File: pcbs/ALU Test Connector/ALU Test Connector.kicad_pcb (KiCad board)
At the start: 2 copper layers, 137.2 x 137.2 mm, 6 parts, among them J1 Conn_02x20_Odd_Even, J2 Conn_02x20_Odd_Even, J3 Conn_01x04

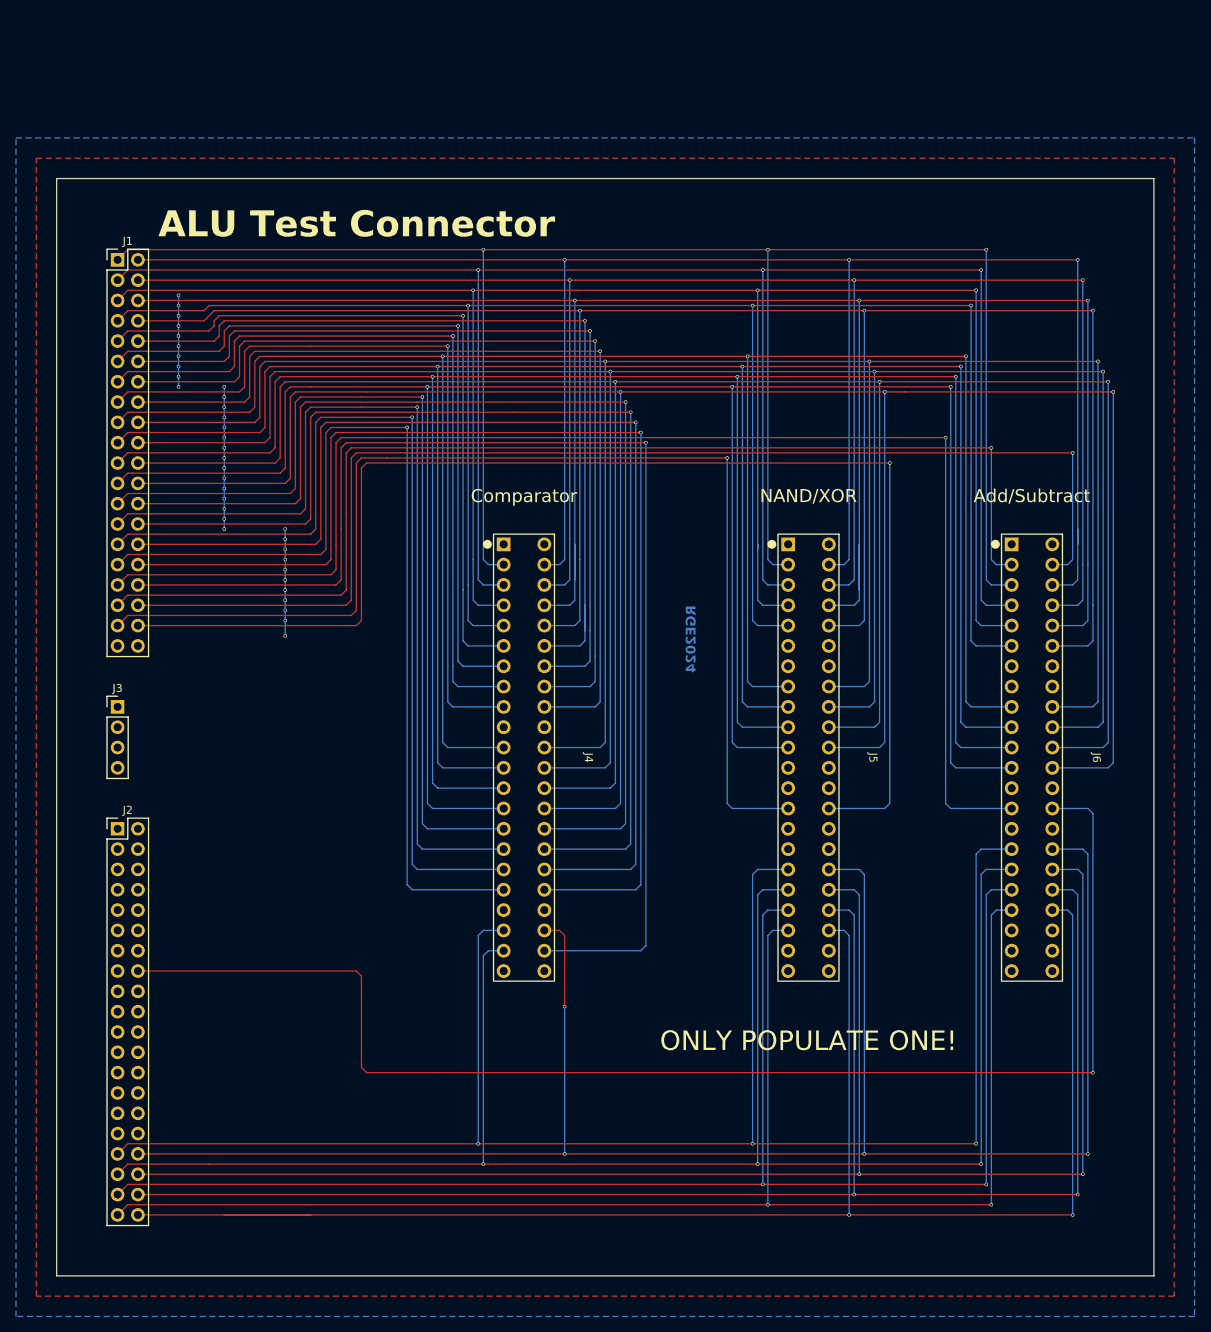
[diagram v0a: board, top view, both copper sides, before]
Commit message: Add alternative power connector
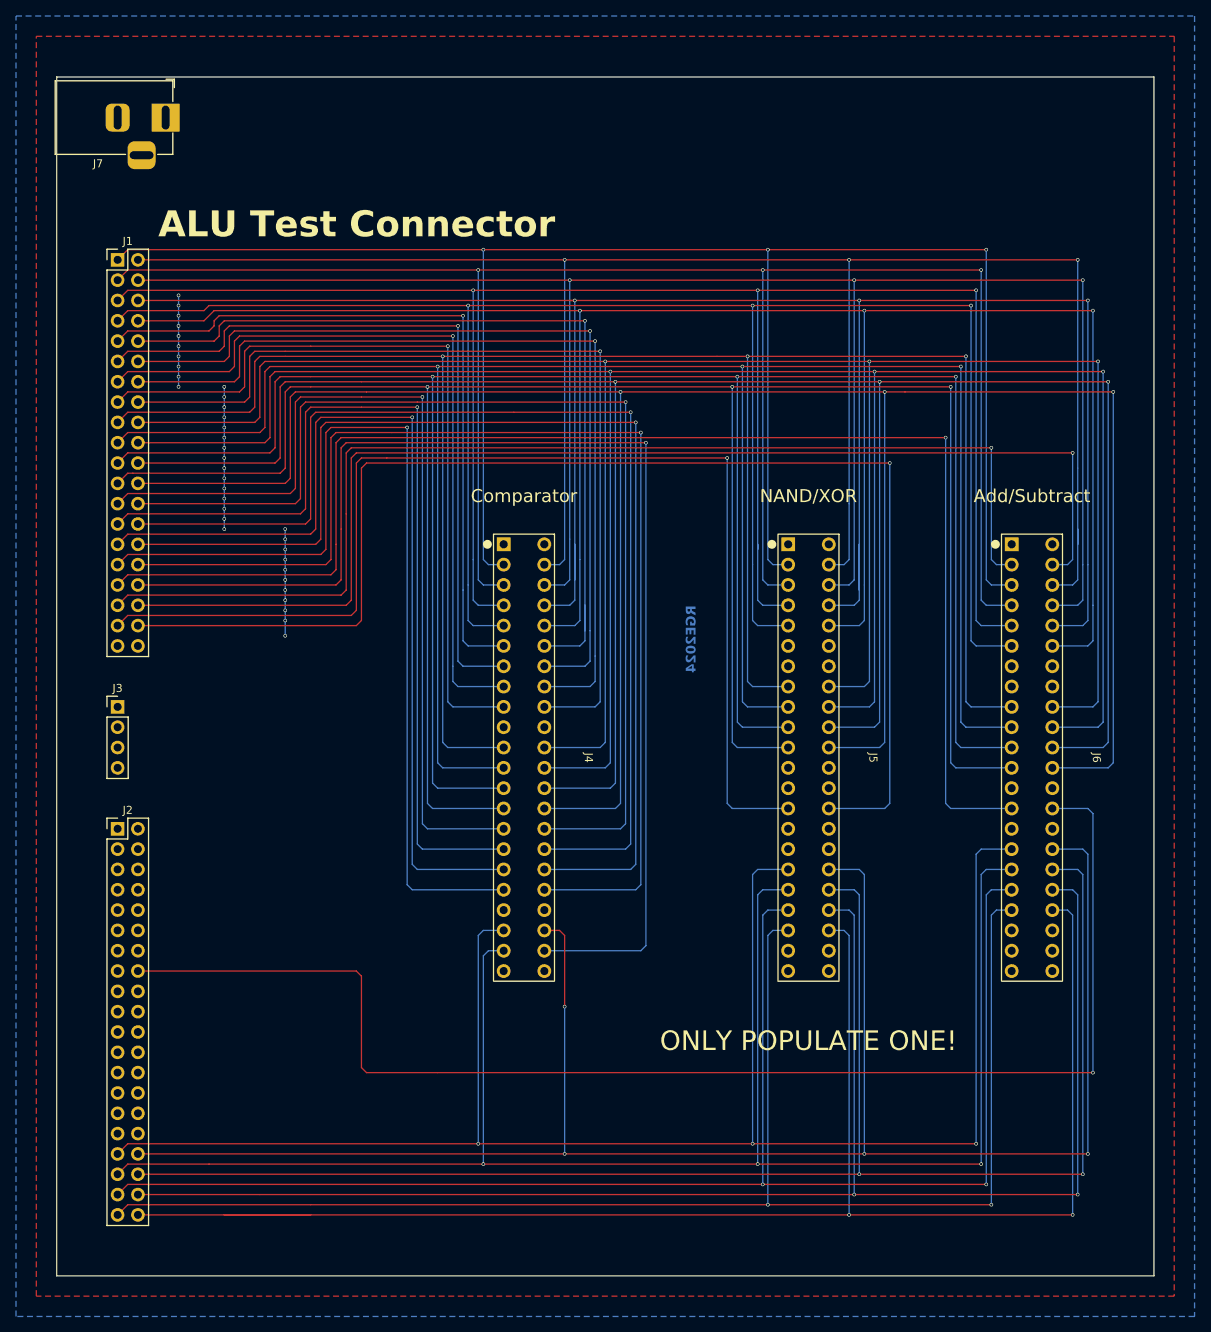
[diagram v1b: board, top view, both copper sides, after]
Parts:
- added J7: Barrel_Jack_Switch, Connector_BarrelJack:BarrelJack_Horizontal, F.Cu at (64.4, 33.0)
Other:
- board size 137.2 x 137.2 mm -> 137.2 x 149.9 mm
